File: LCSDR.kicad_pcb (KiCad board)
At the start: 2 copper layers, 100 x 95 mm, 191 parts, among them J1 Conn_01x10, J10 Conn_01x01, J11 Conn_01x01, J2 Conn_01x10, J3 phones, J4 MIC_PTT, J5 Conn_01x10, J6 Conn_Coaxial, J7 Conn_01x10, J8 Conn_01x01, J9 Conn_01x01, K1 FRT5, K2 FRT5, K3 FRT5, K4 FRT5, Q1 MMBT2222LT1G, Q2 BC847, Q3 MMBT2222LT1G, Q4 MMBT2222LT1G, Q5 Si2301, Q6 Si2301, U1 4053, U10 NE5532, U11 MC33079, U2 74LVC1G00DCKR, U3 4053, U4 74LVC1G00DCKR, U5 FSA3157, U6 NE5532, U7 FSA3157, U8 74LCX574

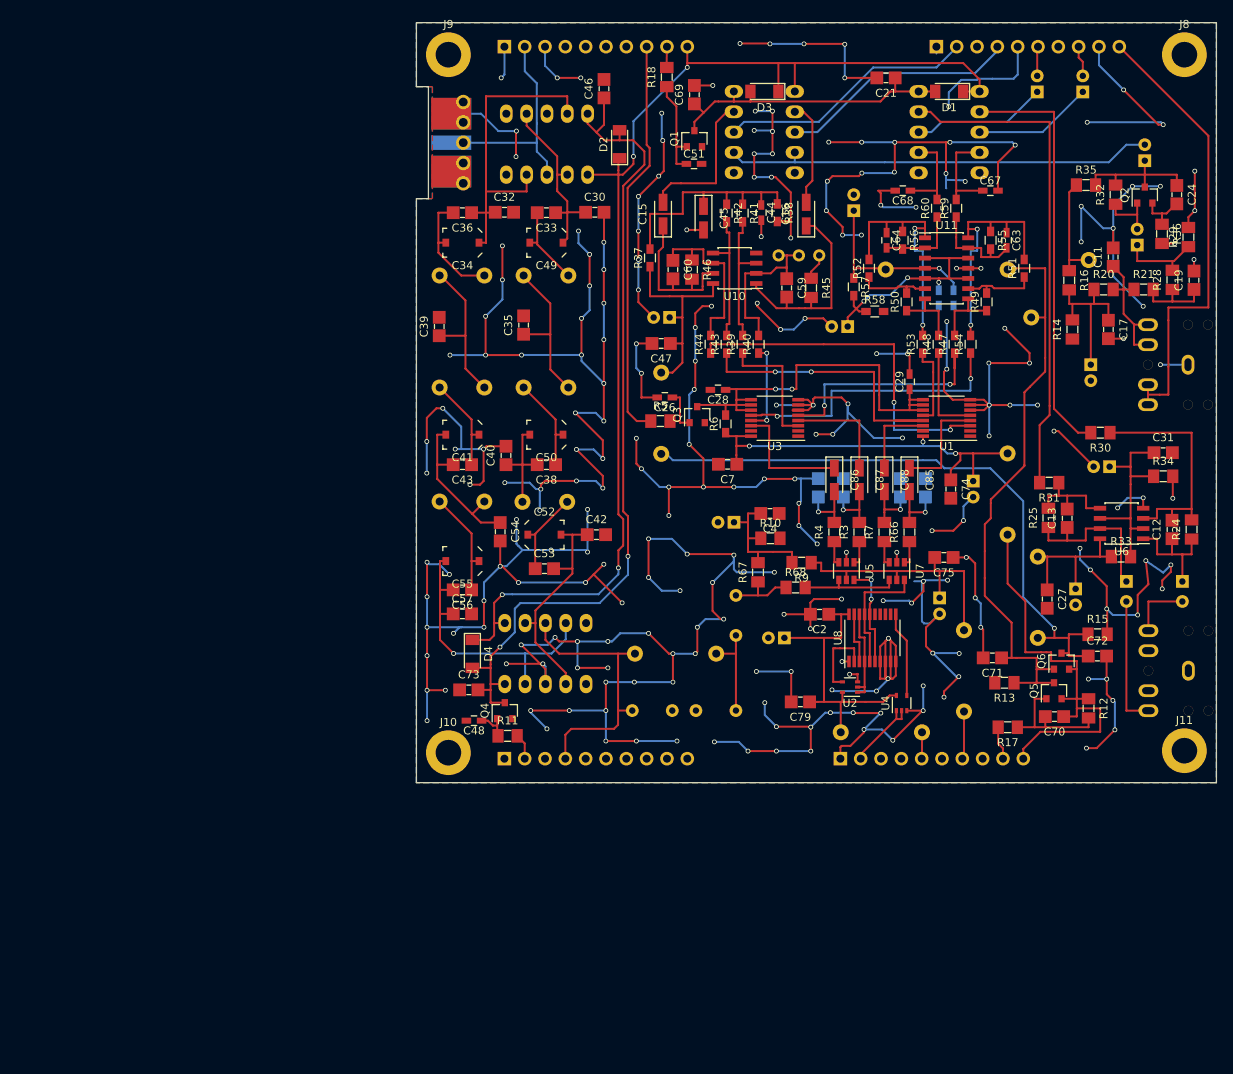
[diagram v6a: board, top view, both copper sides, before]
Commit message: PCB 74LCX574
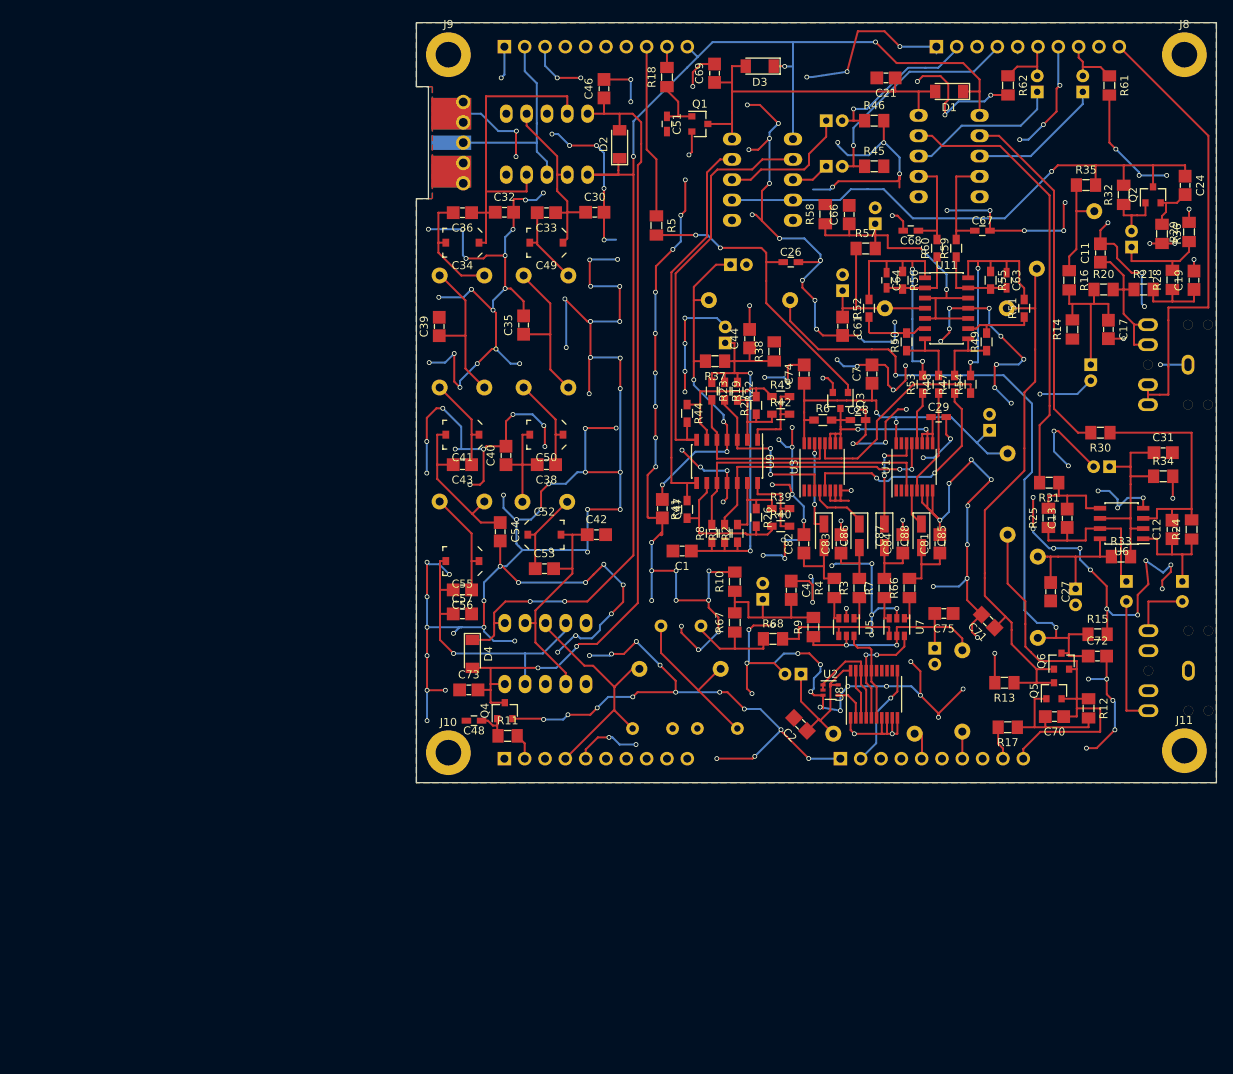
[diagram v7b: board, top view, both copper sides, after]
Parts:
- removed C37: 1uF, Capacitors_THT:CP_Radial_D5.0mm_P2.00mm
- removed C59, C60: 220, UI:C_1206_0603
- removed C79: 100nF, UI:C_1206_0603
- removed RV1: 5k, UI:Potentiometer_Bourns_3296W_3-8Zoll_Inline_ScrewUp
- removed U10: NE5532, Housings_SOIC:SOIC-8_3.9x4.9mm_Pitch1.27mm
- removed U4: 74LVC1G00DCKR, TO_SOT_Packages_SMD:SOT-353_SC-70-5
- added C1: 100nF, UI:C_1206_0603, F.Cu at (148.2, 106.0)
- added R1: 3k, Resistors_SMD:R_0603_HandSoldering, F.Cu at (153.5, 103.8)
- added R19: 3k, Resistors_SMD:R_0603_HandSoldering, F.Cu at (153.5, 86.1)
- added R2: 3k, Resistors_SMD:R_0603_HandSoldering, F.Cu at (155.1, 103.8)
- added R22: 3k, Resistors_SMD:R_0603_HandSoldering, F.Cu at (155.1, 86.1)
- added R23: 3k, Resistors_SMD:R_0603_HandSoldering, F.Cu at (151.9, 86.0)
- added R26: 270, Resistors_SMD:R_0603_HandSoldering, F.Cu at (157.5, 101.8)
- added R27: 270, Resistors_SMD:R_0603_HandSoldering, F.Cu at (157.5, 87.8)
- added R61: 10k, UI:R_1206_0603, F.Cu at (201.6, 47.9)
- added R62: 10k, UI:R_1206_0603, F.Cu at (188.9, 47.8)
- added R8: 3k, Resistors_SMD:R_0603_HandSoldering, F.Cu at (151.9, 103.8)
- added U9: MC33079, Housings_SOIC:SOIC-14_3.9x8.7mm_Pitch1.27mm, F.Cu at (153.8, 94.8)
- C15, C16, C45: footprint Capacitors_Tantalum_SMD:CP_Tantalum_Case-A_EIA-3216-18_Wave -> Capacitors_THT:CP_Radial_D5.0mm_P2.00mm; moved to B.Cu
- C44: footprint Capacitors_SMD:C_0603_HandSoldering -> UI:C_1206_0603
- C61, C66: footprint Capacitors_SMD:C_0603_HandSoldering -> UI:C_1206_0603; moved to F.Cu
- C81, C82, C83, C84: moved to F.Cu
- R37, R38: value 1k -> 750; footprint Resistors_SMD:R_0603_HandSoldering -> UI:R_1206_0603
- R41: value 22k -> 3k
- R42: value 22k -> 1k
- R44: value 1k -> 3k
- R45: value 20k -> 10k
- R46: value 22k -> 10k
- R57, R58: footprint Resistors_SMD:R_0603_HandSoldering -> UI:R_1206_0603
- moved R41 37.7 mm to (148.8, 100.8), turned to 90 degrees
- moved R46 29.4 mm to (172.2, 52.2), turned to 0 degrees
- moved R42 26.0 mm to (160.5, 88.9), turned to 0 degrees
- moved R5 24.5 mm to (145.0, 65.3), turned to 270 degrees
- moved C15 23.5 mm to (166.2, 52.2), turned to 0 degrees
- moved C74 23.3 mm to (163.5, 83.9), turned to 90 degrees
- moved C26 23.1 mm to (161.8, 69.9), turned to 0 degrees
- moved R40 22.9 mm to (160.5, 102.9), turned to 0 degrees
- moved C7 21.3 mm to (171.9, 83.9), turned to 90 degrees
- moved R39 21.1 mm to (160.5, 100.7), turned to 0 degrees
- moved C47 20.7 mm to (145.7, 100.8), turned to 270 degrees
- moved L7 18.1 mm to (156.7, 74.7), turned to 180 degrees
- moved Q3 18.0 mm to (168.0, 87.2), turned to 270 degrees
- moved C28 17.9 mm to (170.2, 89.7), turned to 0 degrees
- moved R38 17.4 mm to (159.7, 81.1), turned to 90 degrees
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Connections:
- C15 pad 1: I_IN -> Net-(C15-Pad1)
- C15 pad 2: Net-(C15-Pad2) -> LINE_IN_LEFT
- C16 pad 1: Q_IN -> Net-(C16-Pad1)
- C16 pad 2: Net-(C16-Pad2) -> LINE_IN_RIGHT
- C44 pad 1: Net-(C44-Pad1) -> Net-(C1-Pad1)
- C45 pad 1: Net-(C44-Pad1) -> Net-(C1-Pad1)
- K2 pad 2: Net-(C16-Pad2) -> Q_IN
- K2 pad 3: LINE_IN_RIGHT -> Net-(C16-Pad1)
- K2 pad 4: Net-(C37-Pad2) -> Net-(C24-Pad1)
- K2 pad 7: Net-(C37-Pad2) -> Net-(C24-Pad1)
- K2 pad 8: LINE_IN_LEFT -> Net-(C15-Pad1)
- K2 pad 9: Net-(C15-Pad2) -> I_IN
- R37 pad 1: Net-(C47-Pad1) -> Net-(C1-Pad1)
- R37 pad 2: Net-(C44-Pad1) -> Net-(C47-Pad1)
- R38 pad 1: Net-(C44-Pad1) -> Net-(C1-Pad1)
- R39 pad 1: RX_0 -> Net-(R2-Pad2)
- R40 pad 1: RX_180 -> Net-(R26-Pad2)
- R40 pad 2: Net-(C59-Pad1) -> Net-(R39-Pad2)
- R41 pad 1: Net-(C44-Pad1) -> Net-(R26-Pad2)
- R41 pad 2: Net-(R39-Pad2) -> I_IN
- R42 pad 1: Net-(C44-Pad1) -> Net-(R22-Pad2)
- R43 pad 1: RX_270 -> Net-(R27-Pad2)
- R44 pad 1: RX_90 -> Net-(R27-Pad2)
- R44 pad 2: Net-(C60-Pad1) -> Q_IN
- R45 pad 1: Net-(R45-Pad1) -> LINE_IN_RIGHT
- R45 pad 2: Q_IN -> GND
- R46 pad 1: Net-(C60-Pad1) -> LINE_IN_LEFT
- R46 pad 2: I_IN -> GND
- U8 pad 11: Net-(U4-Pad4) -> CLK
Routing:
- net GND: track 1039.3 -> 1138.4 mm, vias 237 -> 265
- net Net-(C37-Pad2): track 54.1 -> 0.00 mm
- net Net-(C1-Pad1): track 0.00 -> 54.0 mm, vias 0 -> 2
- net Net-(C24-Pad1): track 17.4 -> 70.6 mm, vias 0 -> 1
- net Net-(C26-Pad1): track 6.55 -> 38.5 mm, vias 0 -> 2
- net I_IN: track 19.8 -> 51.7 mm
- net Net-(C44-Pad1): track 30.8 -> 0.00 mm
- net S1_RX_TX: track 50.3 -> 21.7 mm
- net Q_IN: track 26.5 -> 53.0 mm
- net Net-(C28-Pad1): track 53.9 -> 28.8 mm
- net Net-(C60-Pad1): track 21.6 -> 0.00 mm
- net Net-(C59-Pad1): track 20.4 -> 0.00 mm
- net Net-(C15-Pad2): track 19.8 -> 0.00 mm
- net Net-(R26-Pad2): track 0.00 -> 19.1 mm
- net Net-(R27-Pad2): track 0.00 -> 18.6 mm
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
